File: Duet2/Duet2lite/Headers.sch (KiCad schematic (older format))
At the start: 48 parts, among them J1 EXPANSION, J10 E0 MOT, J11 E0 HEAT, J12 E0 TEMP, J13 E1 HEAT, J14 E1 TEMP, J16 CONN_ALT_HEADER, J19 Z_STOP, J2 FAN2, J20 5V_PS, J23 VIN, J24 GND V_IN, J25 FAN0, J28 Probe, J29 FAN1, J30 PanelDUE, J31 GND V_IN, J32 Y_STOP, J33 X_STOP, J34 E0_STOP, J35 E1_STOP, J36 Z A, J37 SPI0, J39 ESP_COMMS, J4 BED HEAT, J5 BED TEMP, J6 E1 MOT, J7 Z B, J8 Y MOT, J9 X MOT, P1 CONN_SD, P2 CONN_LCD

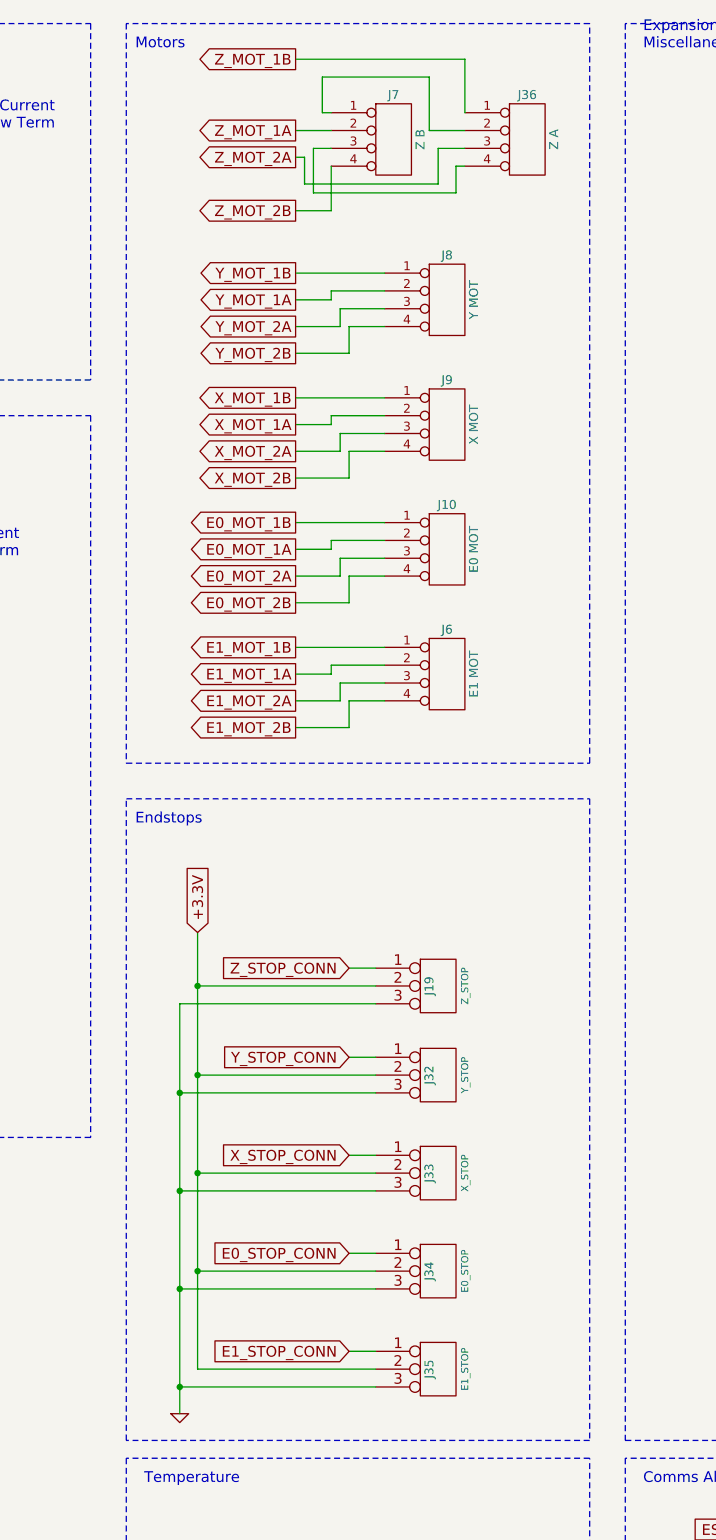
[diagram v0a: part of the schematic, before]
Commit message: removed stepper drivers from the schematic
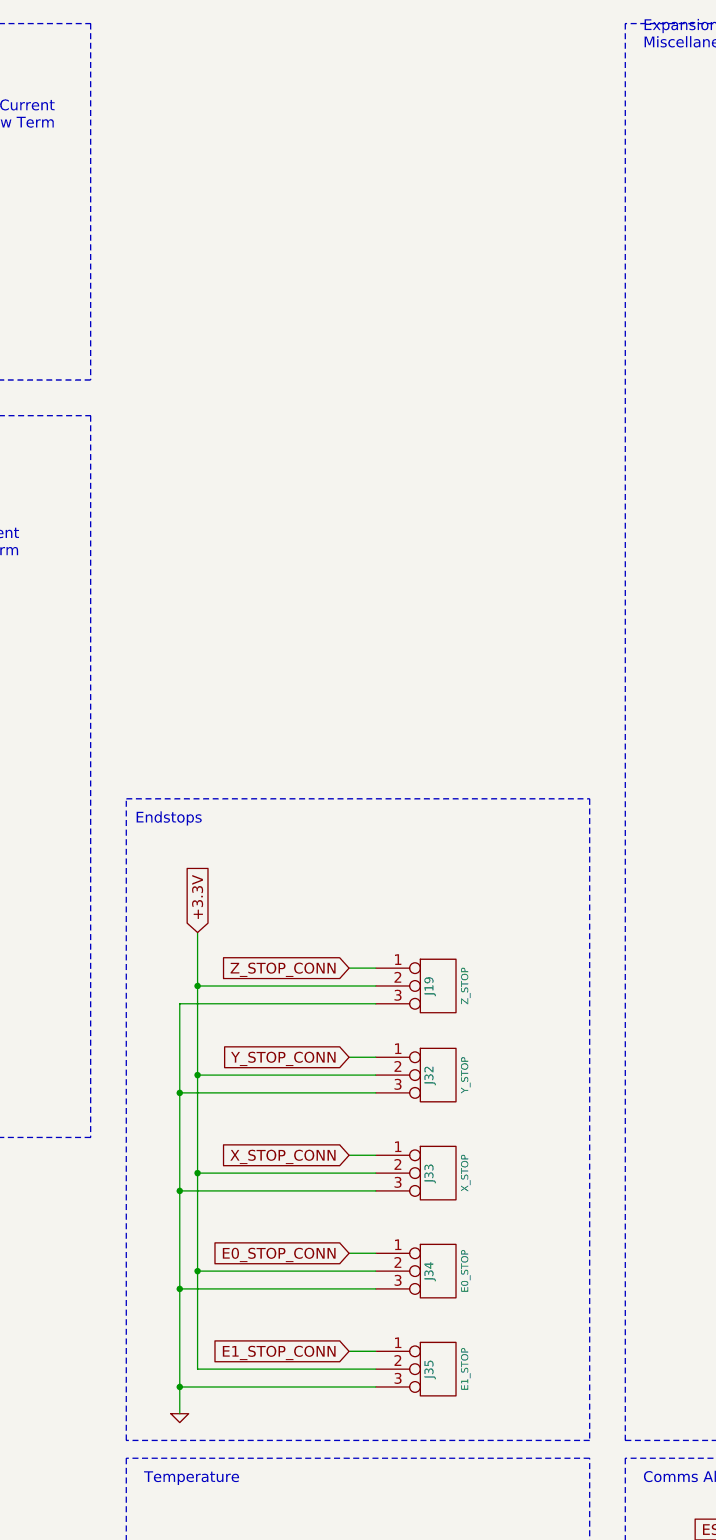
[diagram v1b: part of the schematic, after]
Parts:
- removed J10: E0 MOT, FE Footprints:PIN_ARRAY_4x1, symbol DuetWifi:CONN4
- removed J36: Z A, FE Footprints:PIN_ARRAY_4x1, symbol DuetWifi:CONN4
- removed J6: E1 MOT, FE Footprints:PIN_ARRAY_4x1, symbol DuetWifi:CONN4
- removed J7: Z B, FE Footprints:PIN_ARRAY_4x1, symbol DuetWifi:CONN4
- removed J8: Y MOT, FE Footprints:PIN_ARRAY_4x1, symbol DuetWifi:CONN4
- removed J9: X MOT, FE Footprints:PIN_ARRAY_4x1, symbol DuetWifi:CONN4
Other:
- note removed: "Motors"
